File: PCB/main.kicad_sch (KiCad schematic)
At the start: 64 parts, among them J1 S20B-PADSS-1, J2 S20B-PADSS-1, J3 SWD, SW1 SPST, U1 TPS5430, U2 AMS1117-3.3, U3 MCP2558FD, U4 MCP2558FD, U5 STM32G0B1, Y1 ${Frequency}

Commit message: Add JLCJLCJLCJLC placeholder artwork
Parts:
- added ART3: JLCJLCJLCJLC, libdb:CMP-0047, symbol 0 LibDB:Artwork/CMP-0047
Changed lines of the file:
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@@
+    )
+  )
+  (symbol (lib_id "0 LibDB:Artwork/CMP-0047") (at 246.38 25.4 0) (unit 1)
+    (in_bom no) (on_board yes) (dnp no) (fields_autoplaced)
+    (property "Reference" "ART3" (at 254 24.635 0)
+      (effects (font (size 1.27 1.27)) (justify left))
+    )
+    (property "Value" "JLCJLCJLCJLC" (at 254 27.175 0)
+      (effects (font (size 1.27 1.27)) (justify left))
+    )
+    (property "Footprint" "libdb:CMP-0047" (at 246.38 16.51 0)
+      (effects (font (size 1.27 1.27)) hide)
+    )
+    (property "Datasheet" "" (at 246.38 16.51 0)
+      (effects (font (size 1.27 1.27)) hide)
+    )
+    (instances
+      (project "main"
+        (path "/4f4cf64f-c95a-4a4a-b388-e87470ab2a3e"
+          (reference "ART3") (unit 1)
+        )
+      )
     )
   )

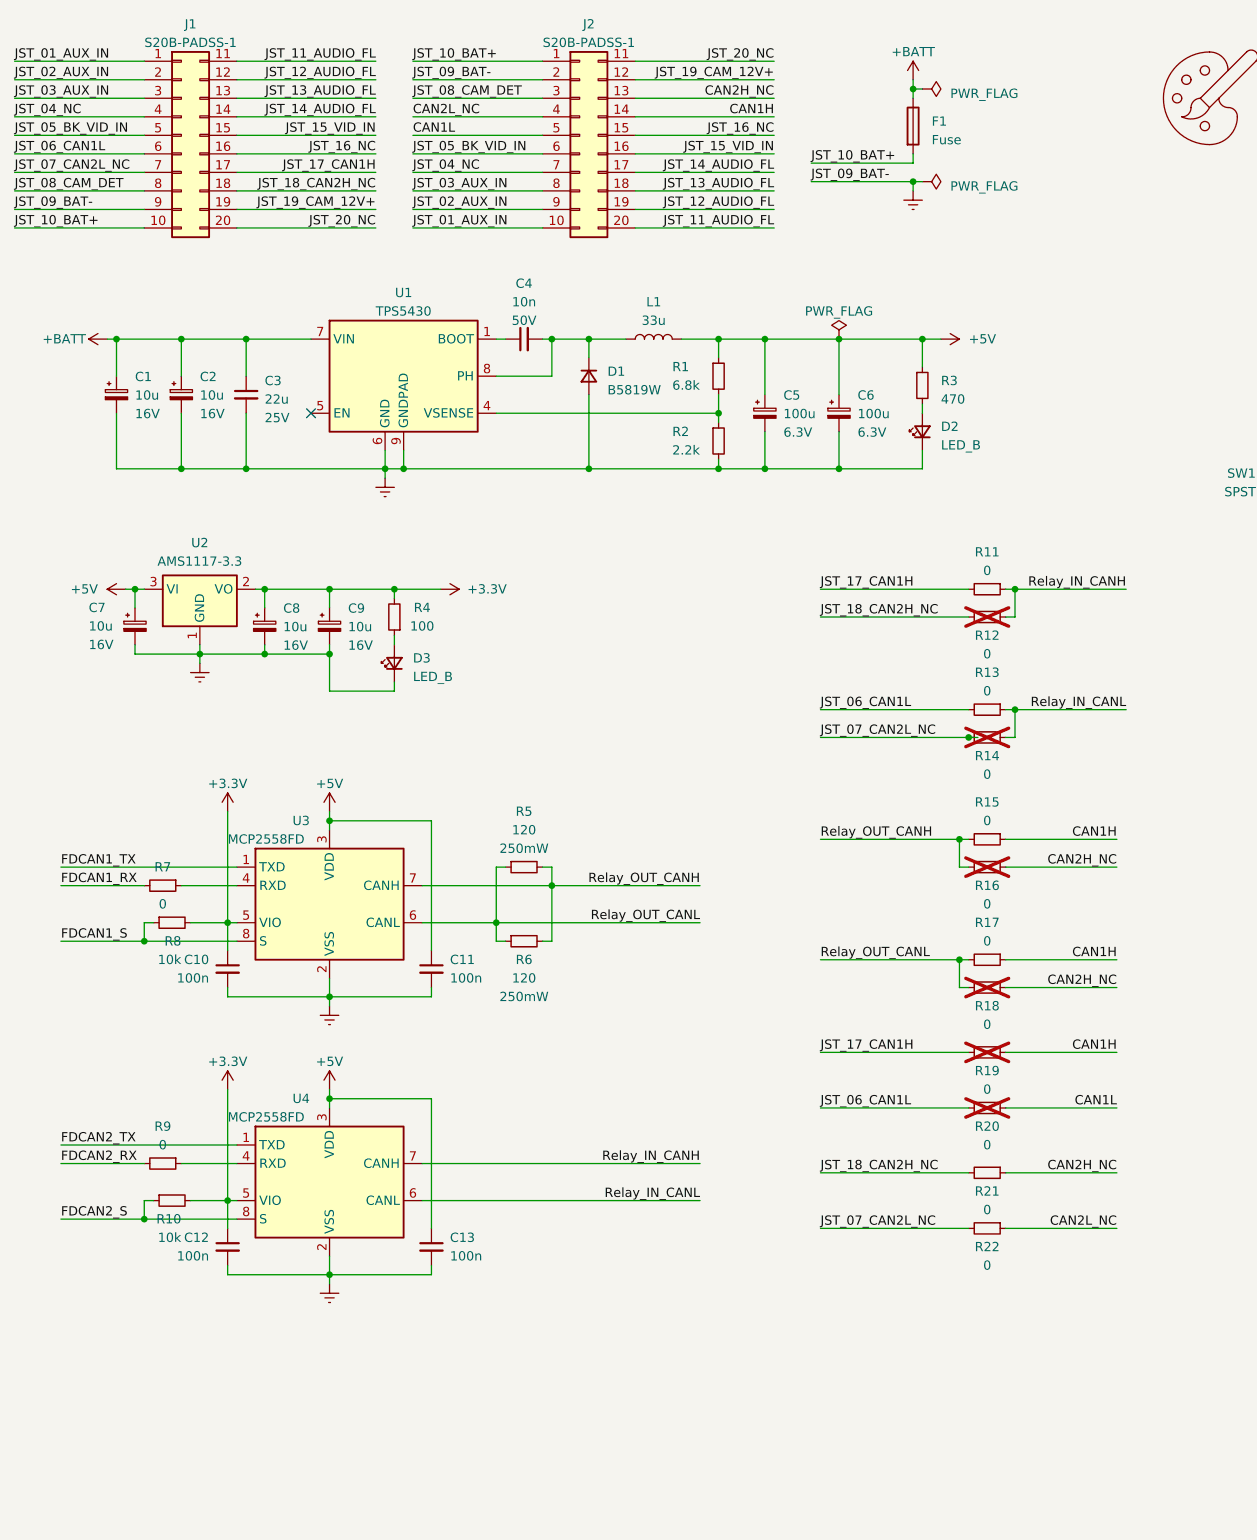
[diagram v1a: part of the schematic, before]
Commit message: Start layout, but intend to ditch the 0ohm resistors and be confident CAN1 is the right one (remember 0402 links)
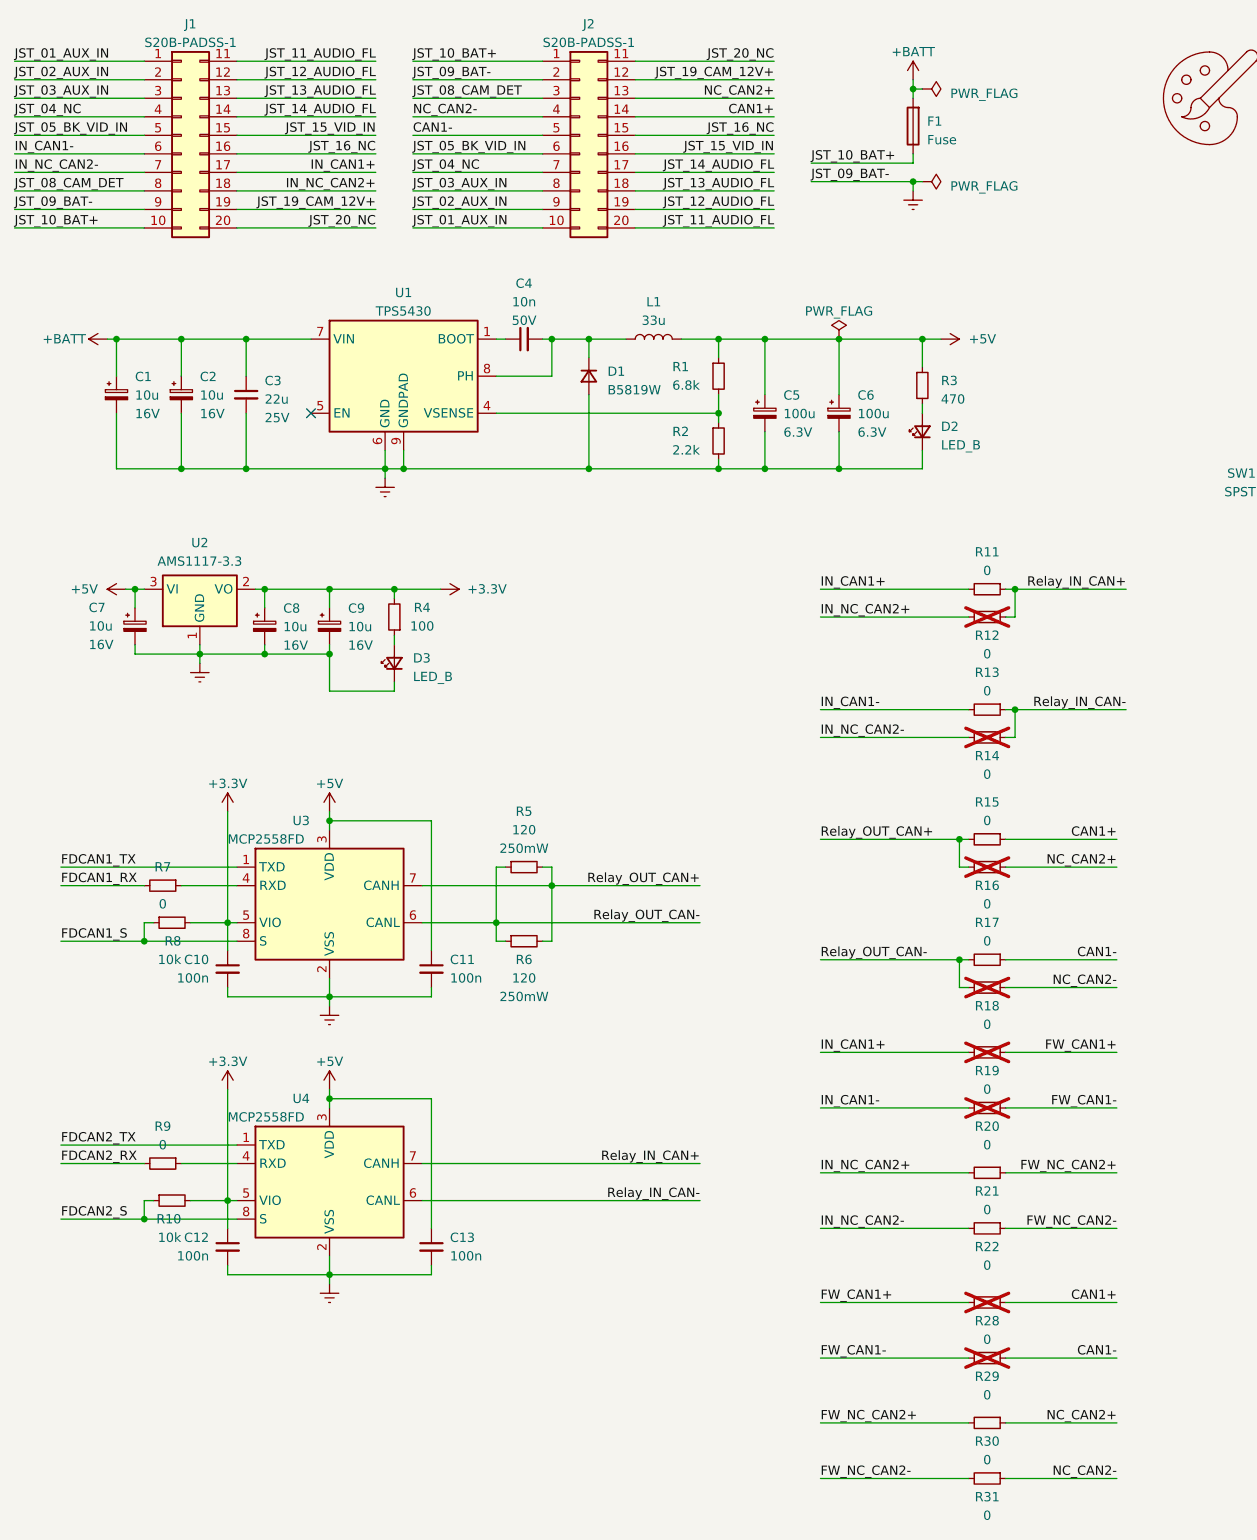
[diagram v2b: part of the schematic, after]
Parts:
- added R28, R29, R30, R31: ${Resistance}, Resistor_SMD:R_0603_1608Metric, symbol 0 LibDB:Resistors/CMP-0048
- R11, R13, R15, R17, R21, R22: footprint Resistor_SMD:R_0402_1005Metric -> Resistor_SMD:R_0603_1608Metric; symbol 0 LibDB:Resistors/CMP-0007 -> 0 LibDB:Resistors/CMP-0048; Case/Package Size 0402 -> 0603; LCSC C17168 -> C21189; MPN 0402WGF0000TCE -> 0603WAF0000T5E; Power Rating 62.5mW -> 100mW
- R12, R14, R16, R18, R19, R20: footprint Resistor_SMD:R_0402_1005Metric -> Resistor_SMD:R_0603_1608Metric; symbol 0 LibDB:Resistors/CMP-0007 -> 0 LibDB:Resistors/CMP-0048; Case/Package Size 0402 -> 0603; LCSC C17168 -> C21189; MPN 0402WGF0000TCE -> 0603WAF0000T5E; Power Rating 62.5mW -> 100mW; now in the parts list
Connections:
- net +BATT: now also F1.2; no longer F1.1
- net JST_10_BAT+: now also F1.1; no longer F1.2
- net CAN1H renamed CAN1+
- net CAN1+: now also R28.1; no longer R17.1, R19.1
- net CAN1L renamed CAN1-
- net CAN1-: now also R17.1, R29.1; no longer R20.1
- net CAN2H_NC renamed NC_CAN2+
- net NC_CAN2+: now also R30.1; no longer R18.1, R21.1
- net CAN2L_NC renamed FW_NC_CAN2-
- net FW_NC_CAN2-: now also R31.2; no longer J2.4 (Pin_4)
- net JST_06_CAN1L renamed IN_CAN1-
- net JST_07_CAN2L_NC renamed IN_NC_CAN2-
- net JST_17_CAN1H renamed IN_CAN1+
- net JST_18_CAN2H_NC renamed IN_NC_CAN2+
- net Relay_IN_CANH renamed Relay_IN_CAN+
- net Relay_IN_CANL renamed Relay_IN_CAN-
- net Relay_OUT_CANH renamed Relay_OUT_CAN+
- net Relay_OUT_CANL renamed Relay_OUT_CAN-
- new net FW_CAN1+: R19.1, R28.2
- new net FW_CAN1-: R20.1, R29.2
- new net FW_NC_CAN2+: R21.1, R30.2
- new net NC_CAN2-: J2.4 (Pin_4), R18.1, R31.1
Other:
- moved on the sheet: F1

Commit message: Start relayout
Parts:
- removed R12, R14, R16, R18, R19, R20, R28, R29, R30, R31: ${Resistance}, Resistor_SMD:R_0603_1608Metric, symbol 0 LibDB:Resistors/CMP-0048
- added R12, R14, R16, R18, R19, R20: ${Resistance}, Resistor_SMD:R_0402_1005Metric, symbol 0 LibDB:Resistors/CMP-0007
- R11, R13, R15, R17, R21, R22: footprint Resistor_SMD:R_0603_1608Metric -> Resistor_SMD:R_0402_1005Metric; symbol 0 LibDB:Resistors/CMP-0048 -> 0 LibDB:Resistors/CMP-0007; Case/Package Size 0603 -> 0402; LCSC C21189 -> C17168; MPN 0603WAF0000T5E -> 0402WGF0000TCE; Power Rating 100mW -> 62.5mW
- U1: footprint Package_SO:TI_SO-PowerPAD-8_ThermalVias -> libdb:CMP-0030
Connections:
- net +BATT: now also F1.1; no longer F1.2
- net JST_10_BAT+: now also F1.2; no longer F1.1
- net NC_CAN2+: now also R12.1
- net NC_CAN2-: now also R14.1
- net Relay_IN_CAN+: now also R16.1; no longer U4.7 (CANH)
- net Relay_IN_CAN-: now also R18.1; no longer U4.6 (CANL)
- net Relay_OUT_CAN+: now also R19.1; no longer R5.2, R6.2, U3.7 (CANH)
- net Relay_OUT_CAN-: now also R20.1; no longer R5.1, R6.1, U3.6 (CANL)
- net PH: now reaches C4.2, D1.1 (K), L1.1, U1.8 (PH)
- net Earth renamed GND
- net FW_NC_CAN2+ renamed FW_CAN2+
- net FW_CAN2+: now also R12.2
- net FW_NC_CAN2- renamed FW_CAN2-
- net FW_CAN2-: now also R14.2
- new net N1+: R19.2, R5.2, R6.2, U3.7 (CANH)
- new net N1-: R20.2, R5.1, R6.1, U3.6 (CANL)
- new net N2+: R16.2, U4.7 (CANH)
- new net N2-: R18.2, U4.6 (CANL)
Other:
- company: (none) -> Richard Carter
- moved on the sheet: F1, R11, R13, R15, R17, R21, R22

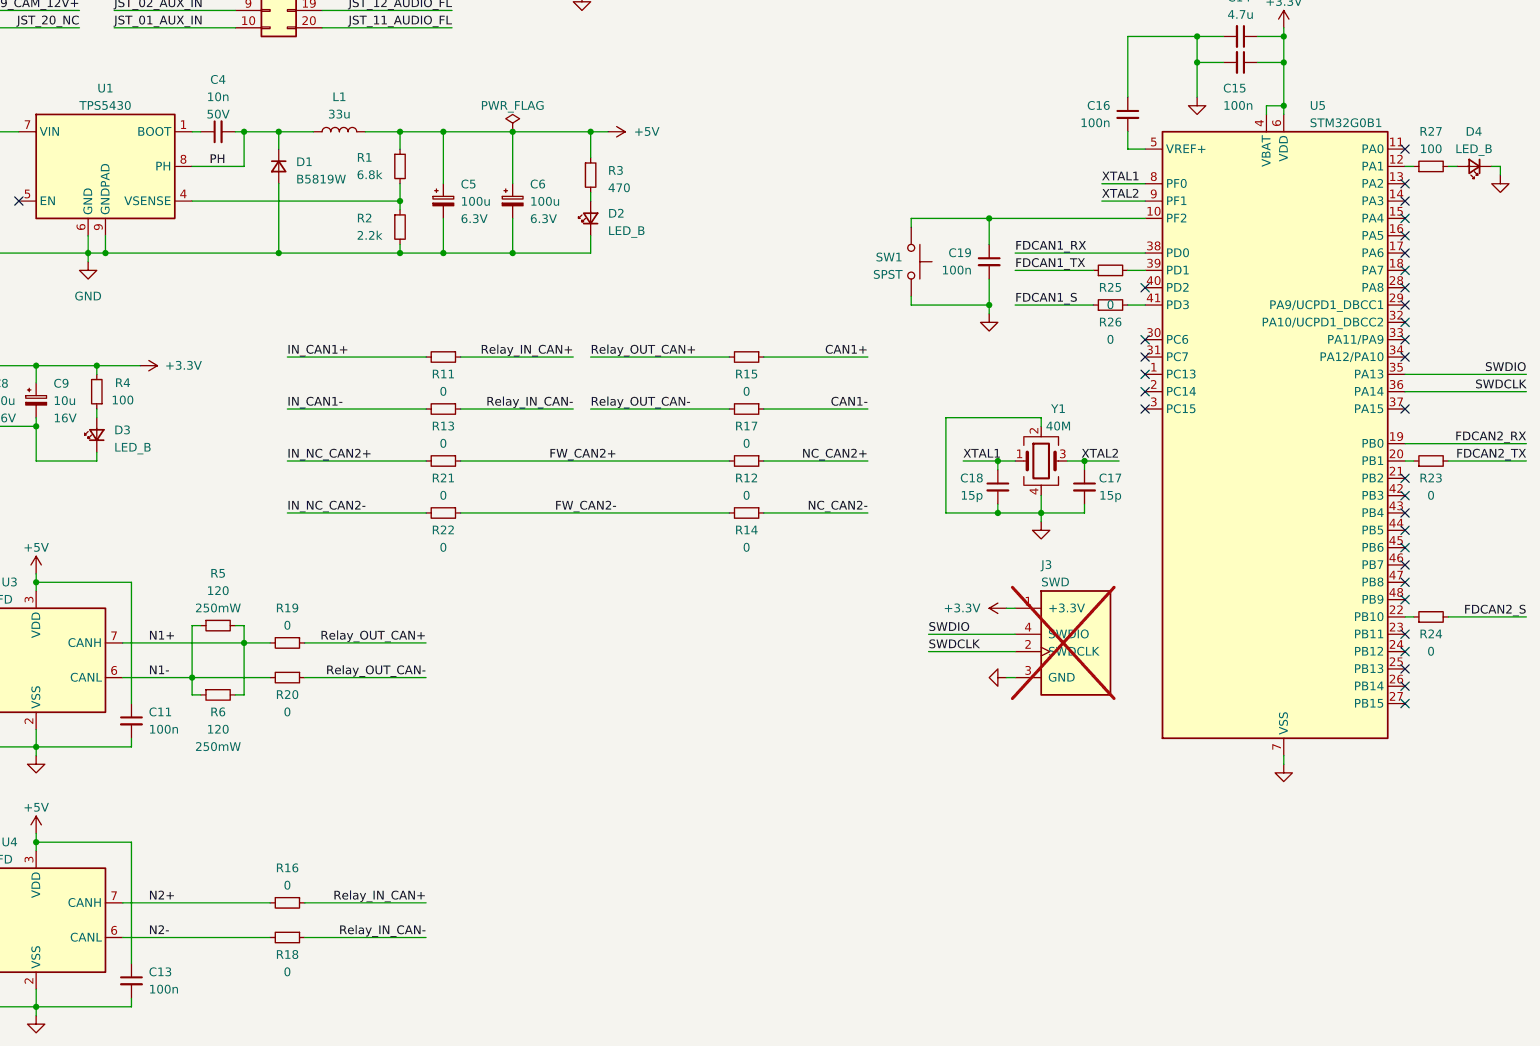
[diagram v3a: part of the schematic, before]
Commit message: Add UART and mostly complete layout
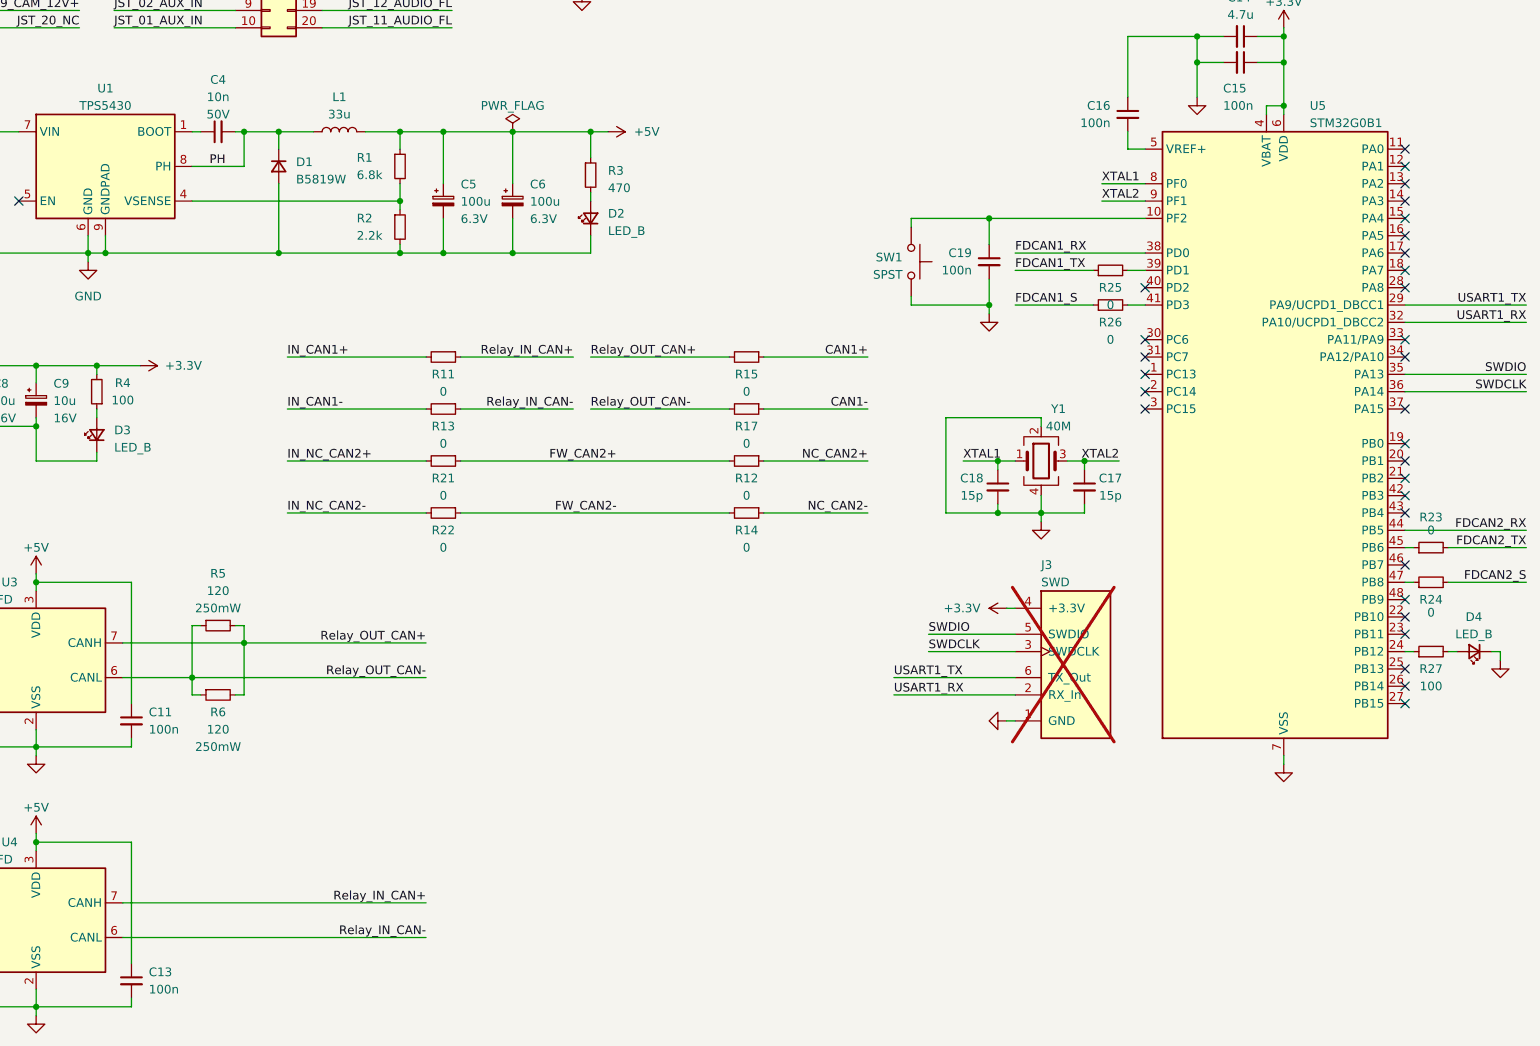
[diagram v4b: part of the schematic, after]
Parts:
- removed R16, R18, R19, R20: ${Resistance}, Resistor_SMD:R_0402_1005Metric, symbol 0 LibDB:Resistors/CMP-0007
- C14: footprint Capacitor_SMD:C_0805_2012Metric -> Capacitor_SMD:C_0603_1608Metric; symbol 0 LibDB:Capacitors/CMP-0009 -> 0 LibDB:Capacitors/CMP-0051; Case/Package Size 0805 -> 0603; LCSC C1779 -> C19666; MPN CL21A475KAQNNNE -> CL10A475KO8NNNC; Voltage Rating 25V -> 16V
- C15, C16, C19: footprint Capacitor_SMD:C_0603_1608Metric -> Capacitor_SMD:C_0402_1005Metric; symbol 0 LibDB:Capacitors/CMP-0008 -> 0 LibDB:Capacitors/CMP-0049; Case/Package Size 0603 -> 0402; LCSC C14663 -> C307331; MPN CC0603KRX7R9BB104 -> CL05B104KB54PNC; Manufacturer Yageo -> Samsung Electro-Mechanics
- J3: footprint libdb:CMP-0022 -> libdb:CMP-0053; symbol 0 LibDB:Connectors/CMP-0022 -> 0 LibDB:Connectors/CMP-0053; now in the parts list
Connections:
- net N1+ is gone; now on net Relay_OUT_CAN+: R5.2, R6.2, U3.7 (CANH)
- net N1- is gone; now on net Relay_OUT_CAN-: R5.1, R6.1, U3.6 (CANL)
- net N2+ is gone; now on net Relay_IN_CAN+: U4.7 (CANH)
- net N2- is gone; now on net Relay_IN_CAN-: U4.6 (CANL)
- net +3.3V: now also J3.4 (+3.3V); no longer J3.1 (+3.3V)
- net FDCAN2_RX: now also U5.44 (PB5); no longer U5.19 (PB0)
- net GND: now also J3.1 (GND); no longer J3.3 (GND)
- net SWDCLK: now also J3.3 (SWDCLK); no longer J3.2 (SWDCLK)
- net SWDIO: now also J3.5 (SWDIO); no longer J3.4 (SWDIO)
- net at R24.1: now also U5.47 (PB8); no longer U5.22 (PB10)
- net at R23.1: now also U5.45 (PB6); no longer U5.20 (PB1)
- net at R27.1: now also U5.24 (PB12); no longer U5.12 (PA1)
- net USART1_TX: now reaches U5.29 (PA9/UCPD1_DBCC1)
- net USART1_TX: now also J3.6 (TX_Out)
- net USART1_RX: now reaches U5.32 (PA10/UCPD1_DBCC2)
- net USART1_RX: now also J3.2 (RX_In)
- no-connect marks 33 -> 31
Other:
- moved on the sheet: D4, R23, R24, R27

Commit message: Remove / from case/package
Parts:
- C1, C2, C3, C7, C8, C9, R5, R6: Case Package Size (none) -> 1206; Case/Package Size 1206 -> (none)
- C10, C11, C12, C13, C15, C16, C17, C18, C19, C4, R1, R10, R11, R12, R13, R14, R15, R17, R2, R21, R22, R23, R24, R25, R26, R27, R3, R4, R7, R8, R9: Case Package Size (none) -> 0402; Case/Package Size 0402 -> (none)
- C14, D2, D3, D4: Case Package Size (none) -> 0603; Case/Package Size 0603 -> (none)
- C5, C6: Case Package Size (none) -> 1210; Case/Package Size 1210 -> (none)
